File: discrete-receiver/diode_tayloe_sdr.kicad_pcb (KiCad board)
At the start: 2 copper layers, 90 x 90 mm, 0 parts

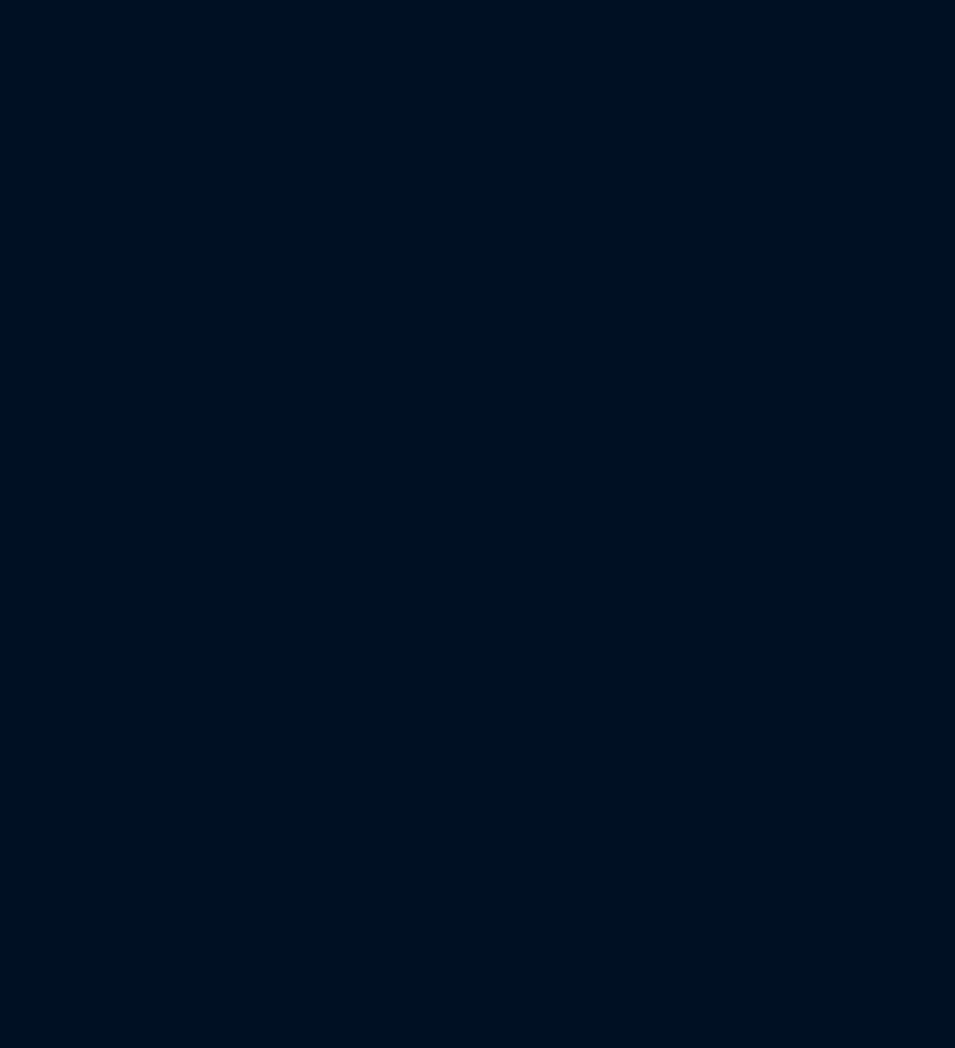
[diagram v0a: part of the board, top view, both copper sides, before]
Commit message: Upgraded to 4 layers, added components. Ready for layout. Only 3 things left on schematic to-do list
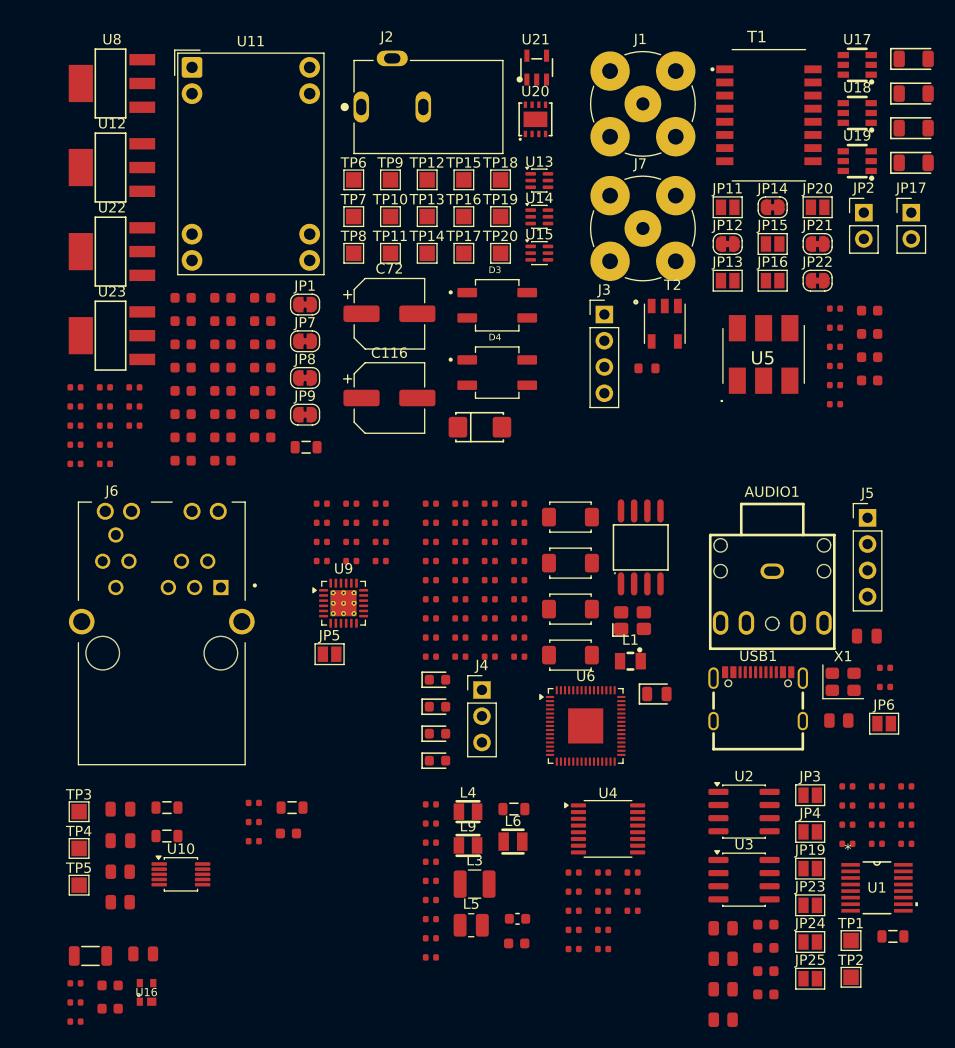
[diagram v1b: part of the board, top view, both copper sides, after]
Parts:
- added AUDIO1: I/Q Out, EasyEDA_Lib:AUDIO-TH_PJ-3126-5A, F.Cu at (215.3, 90.7)
- added C1: 10nF, PCM_JLCPCB:C_0603, F.Cu at (214.7, 122.4)
- added C10: 10uF, PCM_JLCPCB:C_0603, F.Cu at (158.3, 64.0)
- added C100: 100pF, PCM_JLCPCB:C_0603, F.Cu at (168.5, 113.6)
- added C101: 100nF, PCM_JLCPCB:C_0402, F.Cu at (221.4, 66.5)
- added C102: 100pF, PCM_JLCPCB:C_0603, F.Cu at (224.7, 65.3)
- added C103: 100nF, PCM_JLCPCB:C_0402, F.Cu at (221.4, 68.4)
- added C104: 100pF, PCM_JLCPCB:C_0603, F.Cu at (224.7, 67.5)
- added C105: 100nF, PCM_JLCPCB:C_0402, F.Cu at (221.4, 70.2)
- added C106: 100pF, PCM_JLCPCB:C_0603, F.Cu at (224.7, 69.8)
- added C107: 100nF, PCM_JLCPCB:C_0402, F.Cu at (182.3, 125.6)
- added C108: 100pF, PCM_JLCPCB:C_0603, F.Cu at (190.6, 124.2)
- added C109: 10uF, PCM_JLCPCB:C_0603, F.Cu at (166.0, 66.3)
- added C11: 10uF, PCM_JLCPCB:C_0603, F.Cu at (158.3, 66.3)
- added C110: 100nF, PCM_JLCPCB:C_0402, F.Cu at (150.8, 74.1)
- added C111: 100pF, PCM_JLCPCB:C_0603, F.Cu at (166.0, 68.5)
- added C112: 100pF, PCM_JLCPCB:C_0603, F.Cu at (166.0, 70.8)
- added C113: 10uF, PCM_JLCPCB:C_0603, F.Cu at (166.0, 73.0)
- added C114: 100nF, PCM_JLCPCB:C_0402, F.Cu at (150.8, 76.0)
- added C115: 100pF, PCM_JLCPCB:C_0603, F.Cu at (166.0, 75.3)
- added C116: 100uF 25V, Capacitor_SMD:CP_Elec_6.3x7.7, F.Cu at (178.3, 71.5)
- added C12: 100nF, PCM_JLCPCB:C_0805, F.Cu at (154.5, 125.2)
- added C13: 100nF, PCM_JLCPCB:C_0402, F.Cu at (182.3, 81.7)
- added C14: 33pF, PCM_JLCPCB:C_0402, F.Cu at (182.3, 83.5)
- added C15: 4.7uF, PCM_JLCPCB:C_0402, F.Cu at (182.3, 85.4)
- added C16: 4.7uF, PCM_JLCPCB:C_0402, F.Cu at (182.3, 87.2)
- added C17: 33pF, PCM_JLCPCB:C_0402, F.Cu at (182.3, 89.1)
- added C18: 4.7uF, PCM_JLCPCB:C_0402, F.Cu at (182.3, 90.9)
- added C19: 100nF, PCM_JLCPCB:C_0402, F.Cu at (182.3, 92.8)
- added C2: 10nF, PCM_JLCPCB:C_0603, F.Cu at (214.7, 124.7)
- added C20: 4.7uF, PCM_JLCPCB:C_0402, F.Cu at (182.3, 94.6)
- added C21: 100nF, PCM_JLCPCB:C_0402, F.Cu at (182.3, 96.5)
- added C22: 4.7uF, PCM_JLCPCB:C_0402, F.Cu at (185.2, 81.7)
- added C23: 4.7uF, PCM_JLCPCB:C_0402, F.Cu at (185.2, 83.5)
- added C24: 4.7uF, PCM_JLCPCB:C_0402, F.Cu at (185.2, 85.4)
- added C25: 4.7uF, PCM_JLCPCB:C_0402, F.Cu at (185.2, 87.2)
- added C26: 4.7uF, PCM_JLCPCB:C_0402, F.Cu at (185.2, 89.1)
- added C27: 4.7uF, PCM_JLCPCB:C_0402, F.Cu at (185.2, 90.9)
- added C28: 4.7uF, PCM_JLCPCB:C_0402, F.Cu at (185.2, 92.8)
- added C29: 4.7uF, PCM_JLCPCB:C_0402, F.Cu at (185.2, 94.6)
- added C3: 10nF, PCM_JLCPCB:C_0603, F.Cu at (214.7, 126.9)
- added C30: 4.7uF, PCM_JLCPCB:C_0402, F.Cu at (185.2, 96.5)
- added C31: 4.7uF, PCM_JLCPCB:C_0402, F.Cu at (188.0, 81.7)
- added C32: 100pF, PCM_JLCPCB:C_0603, F.Cu at (158.3, 68.5)
- added C33: 100nF, PCM_JLCPCB:C_0402, F.Cu at (147.9, 70.4)
- added C34: 10uF, PCM_JLCPCB:C_0603, F.Cu at (158.3, 70.8)
- added C35: 100nF, PCM_JLCPCB:C_0402, F.Cu at (196.1, 117.4)
- added C36: 1uF, PCM_JLCPCB:C_0402, F.Cu at (196.1, 119.2)
- added C37: 100nF, PCM_JLCPCB:C_0402, F.Cu at (196.1, 121.1)
- added C38: 1uF, PCM_JLCPCB:C_0402, F.Cu at (196.1, 122.9)
- added C39: 100nF, PCM_JLCPCB:C_0402, F.Cu at (196.1, 124.8)
- added C4: 10nF, PCM_JLCPCB:C_0603, F.Cu at (214.7, 129.2)
- added C40: 1uF, PCM_JLCPCB:C_0402, F.Cu at (199.0, 117.4)
- added C41: 100nF, PCM_JLCPCB:C_0402, F.Cu at (199.0, 119.2)
- added C42: 100nF, PCM_JLCPCB:C_0402, F.Cu at (199.0, 121.1)
- added C43: 1uF, PCM_JLCPCB:C_0402, F.Cu at (199.0, 122.9)
- added C44: 100nF, PCM_JLCPCB:C_0402, F.Cu at (199.0, 124.8)
- added C45: 1uF, PCM_JLCPCB:C_0402, F.Cu at (201.8, 117.4)
- added C46: 100nF, PCM_JLCPCB:C_0805, F.Cu at (152.3, 111.2)
- added C47: 100nF, PCM_JLCPCB:C_0805, F.Cu at (152.3, 114.3)
- added C48: 100nF, PCM_JLCPCB:C_0805, F.Cu at (224.5, 94.5)
- added C49: 10pF, PCM_JLCPCB:C_0402, F.Cu at (171.8, 81.7)
- added C5: 100nF, PCM_JLCPCB:C_0402, F.Cu at (222.6, 109.0)
- added C50: 1uF, PCM_JLCPCB:C_0402, F.Cu at (171.8, 83.5)
- added C51: 470pF, PCM_JLCPCB:C_0402, F.Cu at (171.8, 85.4)
- added C52: 1uF, PCM_JLCPCB:C_0402, F.Cu at (171.8, 87.2)
- added C53: 100nF, PCM_JLCPCB:C_0402, F.Cu at (174.6, 81.7)
- added C54: 100nF, PCM_JLCPCB:C_0402, F.Cu at (174.6, 83.5)
- added C55: 100nF, PCM_JLCPCB:C_0402, F.Cu at (147.9, 72.3)
- added C56: 100nF, PCM_JLCPCB:C_0402, F.Cu at (147.9, 128.1)
- added C57: 100nF, PCM_JLCPCB:C_0402, F.Cu at (147.9, 129.9)
- added C58: 51pF, PCM_JLCPCB:C_0402, F.Cu at (182.3, 112.6)
- added C59: 20pF, PCM_JLCPCB:C_0402, F.Cu at (182.3, 114.5)
- added C6: 10pF, PCM_JLCPCB:C_0402, F.Cu at (182.3, 110.8)
- added C60: 10uF, PCM_JLCPCB:C_0603, F.Cu at (158.3, 73.0)
- added C61: 91pF, PCM_JLCPCB:C_0402, F.Cu at (182.3, 116.3)
- added C62: 39pF, PCM_JLCPCB:C_0402, F.Cu at (182.3, 118.2)
- added C63: 68pF, PCM_JLCPCB:C_0402, F.Cu at (182.3, 120.0)
- added C64: 82pF, PCM_JLCPCB:C_0402, F.Cu at (182.3, 121.9)
- added C65: 91pF, PCM_JLCPCB:C_0402, F.Cu at (165.2, 110.6)
- added C66: 91pF, PCM_JLCPCB:C_0402, F.Cu at (165.2, 112.5)
- added C67: 10uF, PCM_JLCPCB:C_0603, F.Cu at (158.3, 75.3)
- added C68: 10uF, PCM_JLCPCB:C_0402, F.Cu at (222.6, 112.7)
- added C69: 1uF, PCM_JLCPCB:C_0402, F.Cu at (222.6, 114.6)
- added C7: 10uF, PCM_JLCPCB:C_0603, F.Cu at (151.3, 128.3)
- added C70: 100nF, PCM_JLCPCB:C_0402, F.Cu at (147.9, 74.1)
- added C71: 100nF, PCM_JLCPCB:C_0402, F.Cu at (147.9, 76.0)
- added C72: 100uF 25V, Capacitor_SMD:CP_Elec_6.3x7.7, F.Cu at (178.3, 63.3)
- added C73: 100pF, PCM_JLCPCB:C_0603, F.Cu at (158.3, 77.5)
- added C74: 100nF, PCM_JLCPCB:C_0402, F.Cu at (147.9, 77.8)
- added C75: 10uF, PCM_JLCPCB:C_0603, F.Cu at (162.2, 61.8)
- added C76: 100pF, PCM_JLCPCB:C_0603, F.Cu at (162.2, 64.0)
- added C77: 100pF, PCM_JLCPCB:C_0603, F.Cu at (162.2, 66.3)
- added C78: 10uF, PCM_JLCPCB:C_0603, F.Cu at (162.2, 68.5)
- added C79: 1uF, PCM_JLCPCB:C_0402, F.Cu at (225.4, 109.0)
- added C8: 100nF, PCM_JLCPCB:C_0402, F.Cu at (222.6, 110.9)
- added C80: 43pF 1%, PCM_JLCPCB:C_0402, F.Cu at (225.4, 110.9)
- added C81: 43pF 1%, PCM_JLCPCB:C_0402, F.Cu at (225.4, 112.7)
- added C82: 1uF, PCM_JLCPCB:C_0402, F.Cu at (225.4, 114.6)
- added C83: 100nF, PCM_JLCPCB:C_0402, F.Cu at (228.3, 109.0)
- added C84: 1uF, PCM_JLCPCB:C_0402, F.Cu at (228.3, 110.9)
- added C85: 100pF, PCM_JLCPCB:C_0603, F.Cu at (162.2, 70.8)
- added C86: 100pF, PCM_JLCPCB:C_0603, F.Cu at (224.7, 63.0)
- added C87: 100nF, PCM_JLCPCB:C_0402, F.Cu at (221.4, 62.8)
- added C88: 100nF, PCM_JLCPCB:C_0402, F.Cu at (147.9, 131.8)
- added C89: 43pF 1%, PCM_JLCPCB:C_0402, F.Cu at (182.3, 123.7)
- added C9: 10uF, PCM_JLCPCB:C_0603, F.Cu at (158.3, 61.8)
- added C90: 100pF, PCM_JLCPCB:C_0603, F.Cu at (162.2, 73.0)
- added C91: 10uF, PCM_JLCPCB:C_0603, F.Cu at (162.2, 75.3)
- added C92: 100nF, PCM_JLCPCB:C_0402, F.Cu at (150.8, 70.4)
- added C93: 100pF, PCM_JLCPCB:C_0603, F.Cu at (162.2, 77.5)
- added C94: 100pF, PCM_JLCPCB:C_0603, F.Cu at (166.0, 61.8)
- added C95: 100nF, PCM_JLCPCB:C_0402, F.Cu at (150.8, 72.3)
- added C96: 10uF, PCM_JLCPCB:C_0603, F.Cu at (166.0, 64.0)
- added C97: 100nF, PCM_JLCPCB:C_0402, F.Cu at (221.4, 64.7)
- added C98: 100pF, PCM_JLCPCB:C_0603, F.Cu at (151.3, 130.5)
- added C99: 100nF, PCM_JLCPCB:C_0402, F.Cu at (165.2, 114.3)
- added D1: Red, PCM_JLCPCB:D_0603, F.Cu at (182.9, 98.7)
- added D10: 1N4004W, PCM_JLCPCB:D_SOD-123FL, F.Cu at (229.0, 42.0)
- added D11: 1N4004W, PCM_JLCPCB:D_SOD-123FL, F.Cu at (229.0, 45.4)
- added D12: 1N4004W, PCM_JLCPCB:D_SOD-123FL, F.Cu at (229.0, 48.7)
- added D13: Green, PCM_JLCPCB:D_0805, F.Cu at (204.2, 100.1)
- added D2: SMAJ58A, PCM_JLCPCB:D_DO-214AC(SMA), F.Cu at (187.1, 74.3)
- added D3: MB10S, sdr_project:SOIC245P670X290-4N, F.Cu at (188.7, 62.5)
- added D4: MB10S, sdr_project:SOIC245P670X290-4N, F.Cu at (188.7, 69.0)
- added D5: Red, PCM_JLCPCB:D_0603, F.Cu at (182.9, 101.3)
- added D7: Red, PCM_JLCPCB:D_0603, F.Cu at (182.9, 103.9)
- added D8: Red, PCM_JLCPCB:D_0603, F.Cu at (182.9, 106.6)
- added D9: 1N4004W, PCM_JLCPCB:D_SOD-123FL, F.Cu at (229.0, 38.7)
- added FB1: ~, PCM_JLCPCB:FB_0805, F.Cu at (227.0, 123.6)
- added FB2: ~, PCM_JLCPCB:FB_0805, F.Cu at (156.8, 111.1)
- added FB4: ~, PCM_JLCPCB:FB_0805, F.Cu at (156.8, 113.8)
- added J1: His Excellence, Connector_Coaxial:BNC_TEConnectivity_1478204_Vertical, F.Cu at (202.8, 43.0)
- added J2: Optional 5V DC Jack, sdr_project:CUI_PJ-102BH, F.Cu at (182.1, 43.3)
- added J3: External Filter, Connector_PinHeader_2.54mm:PinHeader_1x04_P2.54mm_Vertical, F.Cu at (199.1, 63.4)
- added J4: Debug Pins, Connector_PinHeader_2.54mm:PinHeader_1x03_P2.54mm_Vertical, F.Cu at (187.2, 99.7)
- added J5: Display Connector, Connector_PinHeader_2.54mm:PinHeader_1x04_P2.54mm_Vertical, F.Cu at (224.5, 83.1)
- added J6: SI-52003-F, sdr_project:BEL_SI-52003-F, F.Cu at (156.3, 93.1)
- added J7: Her Excellency, Connector_Coaxial:BNC_TEConnectivity_1478204_Vertical, F.Cu at (202.8, 55.1)
- added JP1: 5.65V Jumper, Jumper:SolderJumper-2_P1.3mm_Bridged_RoundedPad1.0x1.5mm, F.Cu at (170.1, 62.4)
- added JP11: SolderJumper_2_Open, Jumper:SolderJumper-2_P1.3mm_Open_Pad1.0x1.5mm, F.Cu at (211.0, 53.0)
- added JP12: SolderJumper_2_Bridged, Jumper:SolderJumper-2_P1.3mm_Bridged_RoundedPad1.0x1.5mm, F.Cu at (211.0, 56.6)
- added JP13: SolderJumper_2_Open, Jumper:SolderJumper-2_P1.3mm_Open_Pad1.0x1.5mm, F.Cu at (211.0, 60.1)
- added JP14: SolderJumper_2_Bridged, Jumper:SolderJumper-2_P1.3mm_Bridged_RoundedPad1.0x1.5mm, F.Cu at (215.4, 53.0)
- added JP15: SolderJumper_2_Open, Jumper:SolderJumper-2_P1.3mm_Open_Pad1.0x1.5mm, F.Cu at (215.4, 56.6)
- added JP16: SolderJumper_2_Open, Jumper:SolderJumper-2_P1.3mm_Open_Pad1.0x1.5mm, F.Cu at (215.4, 60.1)
- added JP17: Jumper_2_Small_Open, Connector_PinHeader_2.54mm:PinHeader_1x02_P2.54mm_Vertical, F.Cu at (228.8, 53.5)
- added JP19: SolderJumper_2_Open, Jumper:SolderJumper-2_P1.3mm_Open_Pad1.0x1.5mm, F.Cu at (219.0, 117.0)
- added JP2: Jumper_2_Small_Open, Connector_PinHeader_2.54mm:PinHeader_1x02_P2.54mm_Vertical, F.Cu at (224.2, 53.5)
- added JP20: SolderJumper_2_Open, Jumper:SolderJumper-2_P1.3mm_Open_Pad1.0x1.5mm, F.Cu at (219.7, 53.0)
- added JP21: SolderJumper_2_Bridged, Jumper:SolderJumper-2_P1.3mm_Bridged_RoundedPad1.0x1.5mm, F.Cu at (219.7, 56.6)
- added JP22: SolderJumper_2_Bridged, Jumper:SolderJumper-2_P1.3mm_Bridged_RoundedPad1.0x1.5mm, F.Cu at (219.7, 60.1)
- added JP23: SolderJumper_2_Open, Jumper:SolderJumper-2_P1.3mm_Open_Pad1.0x1.5mm, F.Cu at (219.0, 120.5)
- added JP24: SolderJumper_2_Open, Jumper:SolderJumper-2_P1.3mm_Open_Pad1.0x1.5mm, F.Cu at (219.0, 124.1)
- added JP25: SolderJumper_2_Open, Jumper:SolderJumper-2_P1.3mm_Open_Pad1.0x1.5mm, F.Cu at (219.0, 127.6)
- added JP3: SolderJumper_2_Open, Jumper:SolderJumper-2_P1.3mm_Open_Pad1.0x1.5mm, F.Cu at (219.0, 109.9)
- added JP4: SolderJumper_2_Open, Jumper:SolderJumper-2_P1.3mm_Open_Pad1.0x1.5mm, F.Cu at (219.0, 113.4)
- added JP5: SolderJumper_2_Open, Jumper:SolderJumper-2_P1.3mm_Open_Pad1.0x1.5mm, F.Cu at (172.5, 96.3)
- added JP6: SolderJumper_2_Open, Jumper:SolderJumper-2_P1.3mm_Open_Pad1.0x1.5mm, F.Cu at (226.1, 103.0)
- added JP7: USB_Jumper, Jumper:SolderJumper-2_P1.3mm_Bridged_RoundedPad1.0x1.5mm, F.Cu at (170.1, 66.0)
- added JP8: DC_Jumper, Jumper:SolderJumper-2_P1.3mm_Bridged_RoundedPad1.0x1.5mm, F.Cu at (170.1, 69.5)
- added JP9: POE_Jumper, Jumper:SolderJumper-2_P1.3mm_Bridged_RoundedPad1.0x1.5mm, F.Cu at (170.1, 73.1)
- added L1: 3.3uH, EasyEDA_Lib:IND-SMD_L2.0-W1.6_AOTA-B201610S3R3-101-T, F.Cu at (201.6, 96.9)
- added L10: 160nH, PCM_JLCPCB:L_0805, F.Cu at (190.3, 111.2)
- added L11: 300nH, PCM_JLCPCB:L_0805, F.Cu at (168.9, 111.1)
- added L12: 2.2uH,50mA, PCM_JLCPCB:L_0805, F.Cu at (170.2, 76.2)
- added L2: 4.7uH,25mA, PCM_JLCPCB:L_1206, F.Cu at (149.4, 125.4)
- added L3: 27nH, Inductor_SMD:L_1210_3225Metric, F.Cu at (186.5, 118.5)
- added L4: 33nH, EasyEDA_Lib:IND-SMD_L2.2-W1.6, F.Cu at (185.9, 111.5)
- added L5: 68nH, Inductor_SMD:L_1008_2520Metric, F.Cu at (186.2, 122.5)
- added L6: 16nH, EasyEDA_Lib:IND-SMD_L2.4-W1.7, F.Cu at (190.2, 114.4)
- added L8: 36nH, PCM_JLCPCB:L_0603, F.Cu at (190.7, 121.9)
- added L9: 18nH, EasyEDA_Lib:IND-SMD_L2.2-W1.6, F.Cu at (185.9, 114.8)
- added R1: 5.1kΩ, PCM_JLCPCB:R_0402, F.Cu at (226.2, 97.6)
- added R10: 10kΩ, PCM_JLCPCB:R_0402, F.Cu at (153.6, 70.4)
- added R11: 330Ω, PCM_JLCPCB:R_0402, F.Cu at (188.0, 94.6)
- added R12: 330Ω, PCM_JLCPCB:R_0402, F.Cu at (188.0, 96.5)
- added R13: 33Ω, PCM_JLCPCB:R_0402, F.Cu at (190.9, 81.7)
- added R14: 47Ω, PCM_JLCPCB:R_0402, F.Cu at (228.3, 112.7)
- added R15: 47Ω, PCM_JLCPCB:R_0402, F.Cu at (228.3, 114.6)
- added R16: 10kΩ, PCM_JLCPCB:R_0402, F.Cu at (190.9, 83.5)
- added R17: 10kΩ, PCM_JLCPCB:R_0402, F.Cu at (190.9, 85.4)
- added R18: 12kΩ, PCM_JLCPCB:R_0402, F.Cu at (174.6, 85.4)
- added R19: 330Ω, PCM_JLCPCB:R_0402, F.Cu at (190.9, 87.2)
- added R2: 1kΩ, PCM_JLCPCB:R_0402, F.Cu at (188.0, 83.5)
- added R20: 10kΩ, PCM_JLCPCB:R_0402, F.Cu at (201.8, 119.2)
- added R21: 10kΩ, PCM_JLCPCB:R_0805, F.Cu at (210.6, 122.8)
- added R22: 10kΩ, PCM_JLCPCB:R_0402, F.Cu at (190.9, 89.1)
- added R23: 4.7kΩ, PCM_JLCPCB:R_0402, F.Cu at (190.9, 90.9)
- added R24: 4.7kΩ, PCM_JLCPCB:R_0402, F.Cu at (190.9, 92.8)
- added R25: 10kΩ, PCM_JLCPCB:R_0402, F.Cu at (174.6, 87.2)
- added R26: 1.5kΩ, PCM_JLCPCB:R_0402, F.Cu at (190.9, 94.6)
- added R27: 10kΩ, PCM_JLCPCB:R_0402, F.Cu at (153.6, 72.3)
- added R28: 10kΩ, PCM_JLCPCB:R_0402, F.Cu at (201.8, 121.1)
- added R29: 10kΩ, PCM_JLCPCB:R_0805, F.Cu at (210.6, 125.7)
- added R3: 49.9kΩ, PCM_JLCPCB:R_0402, F.Cu at (150.8, 77.8)
- added R30: 100Ω, PCM_JLCPCB:R_0402, F.Cu at (177.5, 81.7)
- added R31: 100Ω, PCM_JLCPCB:R_0402, F.Cu at (177.5, 83.5)
- added R32: 10kΩ, PCM_JLCPCB:R_0402, F.Cu at (177.5, 85.4)
- added R33: 10kΩ, PCM_JLCPCB:R_0402, F.Cu at (177.5, 87.2)
- added R34: 33Ω, PCM_JLCPCB:R_0805, F.Cu at (221.8, 102.7)
- added R35: 10kΩ, PCM_JLCPCB:R_0402, F.Cu at (153.6, 74.1)
- added R36: 330Ω, PCM_JLCPCB:R_0402, F.Cu at (190.9, 96.5)
- added R37: 33Ω, PCM_JLCPCB:R_0805, F.Cu at (152.3, 117.3)
- added R38: 33Ω, PCM_JLCPCB:R_0805, F.Cu at (152.3, 120.2)
- added R4: 5.1kΩ, PCM_JLCPCB:R_0402, F.Cu at (226.2, 99.4)
- added R40: 10kΩ, PCM_JLCPCB:R_0805, F.Cu at (210.6, 128.7)
- added R41: 10kΩ, PCM_JLCPCB:R_0805, F.Cu at (210.6, 131.6)
- added R43: 47 1%, PCM_JLCPCB:R_0603, F.Cu at (203.2, 68.6)
- added R46: 10kΩ, PCM_JLCPCB:R_0402, F.Cu at (221.4, 72.1)
- added R5: 1kΩ, PCM_JLCPCB:R_0402, F.Cu at (188.0, 85.4)
- added R6: 10kΩ, PCM_JLCPCB:R_0402, F.Cu at (188.0, 87.2)
- added R7: 1kΩ, PCM_JLCPCB:R_0402, F.Cu at (188.0, 89.1)
- added R8: 47Ω, PCM_JLCPCB:R_0402, F.Cu at (188.0, 90.9)
- added R9: 47Ω, PCM_JLCPCB:R_0402, F.Cu at (188.0, 92.8)
- added S1: Tactile Button, 160gf, PCM_JLCPCB:SW_TS-1088-AR02016, F.Cu at (195.8, 83.0)
- added S2: Tactile Button, 160gf, PCM_JLCPCB:SW_TS-1088-AR02016, F.Cu at (195.8, 87.4)
- added S3: Tactile Button, 160gf, PCM_JLCPCB:SW_TS-1088-AR02016, F.Cu at (195.8, 91.9)
- added S4: Tactile Button, 160gf, PCM_JLCPCB:SW_TS-1088-AR02016, F.Cu at (195.8, 96.3)
- added T1: H1102NLT, sdr_project:XFMR_H1102NLT, F.Cu at (215.0, 44.1)
- added T2: MABA-007159-000000, sdr_project:XFMR_MABA-007159-000000, F.Cu at (204.9, 64.3)
- added TP1: I_out, TestPoint:TestPoint_Pad_1.5x1.5mm, F.Cu at (222.9, 124.0)
- added TP10: +3.3V, TestPoint:TestPoint_Pad_1.5x1.5mm, F.Cu at (178.4, 53.9)
- added TP11: USB_IN, TestPoint:TestPoint_Pad_1.5x1.5mm, F.Cu at (178.4, 57.5)
- added TP12: POE_IN, TestPoint:TestPoint_Pad_1.5x1.5mm, F.Cu at (181.9, 50.4)
- added TP13: +4.8V_A, TestPoint:TestPoint_Pad_1.5x1.5mm, F.Cu at (181.9, 53.9)
- added TP14: +2.4V_A, TestPoint:TestPoint_Pad_1.5x1.5mm, F.Cu at (181.9, 57.5)
- added TP15: +3.3V_ADC, TestPoint:TestPoint_Pad_1.5x1.5mm, F.Cu at (185.5, 50.4)
- added TP16: POE_Raw, TestPoint:TestPoint_Pad_1.5x1.5mm, F.Cu at (185.5, 53.9)
- added TP17: POE+, TestPoint:TestPoint_Pad_1.5x1.5mm, F.Cu at (185.5, 57.5)
- added TP18: POE-, TestPoint:TestPoint_Pad_1.5x1.5mm, F.Cu at (189.0, 50.4)
- added TP19: +3.3V_SI5351, TestPoint:TestPoint_Pad_1.5x1.5mm, F.Cu at (189.0, 53.9)
- added TP2: Q_out, TestPoint:TestPoint_Pad_1.5x1.5mm, F.Cu at (222.9, 127.5)
- added TP20: +3.3V_CLK, TestPoint:TestPoint_Pad_1.5x1.5mm, F.Cu at (189.0, 57.5)
- added TP3: I LO, TestPoint:TestPoint_Pad_1.5x1.5mm, F.Cu at (148.3, 111.5)
- added TP4: Q LO, TestPoint:TestPoint_Pad_1.5x1.5mm, F.Cu at (148.3, 115.0)
- added TP5: OSC, TestPoint:TestPoint_Pad_1.5x1.5mm, F.Cu at (148.3, 118.6)
- added TP6: DC_IN, TestPoint:TestPoint_Pad_1.5x1.5mm, F.Cu at (174.8, 50.4)
- added TP7: VIN, TestPoint:TestPoint_Pad_1.5x1.5mm, F.Cu at (174.8, 53.9)
- added TP8: GND, TestPoint:TestPoint_Pad_1.5x1.5mm, F.Cu at (174.8, 57.5)
- added TP9: +5V, TestPoint:TestPoint_Pad_1.5x1.5mm, F.Cu at (178.4, 50.4)
- added U1: SN74CBT3253DBQR, sdr_project:SN74CBT3253DBQ16, F.Cu at (225.5, 118.9)
- added U10: MS5351M, Package_SO:MSOP-10_3x3mm_P0.5mm, F.Cu at (158.1, 117.5)
- added U11: Ag9905LP, Converter_DCDC:Converter_DCDC_Silvertel_Ag99xxLP_THT, F.Cu at (159.2, 39.5)
- added U12: ~, EasyEDA_Lib:SOT-223-3_L6.5-W3.4-P2.30-LS7.0-BR, F.Cu at (151.4, 49.2)
- added U13: LM66100DCK, Package_TO_SOT_SMD:SOT-363_SC-70-6, F.Cu at (192.8, 50.4)
- added U14: LM66100DCK, Package_TO_SOT_SMD:SOT-363_SC-70-6, F.Cu at (192.8, 54.0)
- added U15: LM66100DCK, Package_TO_SOT_SMD:SOT-363_SC-70-6, F.Cu at (192.8, 57.5)
- added U16: PSA4-5043_, sdr_project:PSA4-5043_, F.Cu at (154.8, 129.0)
- added U17: ~, EasyEDA_Lib:SOT-23-6_L2.9-W1.6-P0.95-LS2.8-BR, F.Cu at (223.5, 39.3)
- added U18: ~, EasyEDA_Lib:SOT-23-6_L2.9-W1.6-P0.95-LS2.8-BR, F.Cu at (223.5, 43.9)
- added U19: ~, EasyEDA_Lib:SOT-23-6_L2.9-W1.6-P0.95-LS2.8-BR, F.Cu at (223.5, 48.6)
- added U2: OPA1612AxD, Package_SO:SOIC-8_3.9x4.9mm_P1.27mm, F.Cu at (212.6, 111.5)
- added U20: ~, EasyEDA_Lib:TDFN-8_L3.0-W3.0-P0.65-BL-EP2.3, F.Cu at (192.4, 44.5)
- added U21: ~, EasyEDA_Lib:SOT-23-5_L3.0-W1.7-P0.95-LS2.8-BL, F.Cu at (192.5, 39.5)
- added U22: ~, EasyEDA_Lib:SOT-223-3_L6.5-W3.4-P2.30-LS7.0-BR, F.Cu at (151.4, 57.3)
- added U23: ~, EasyEDA_Lib:SOT-223-3_L6.5-W3.4-P2.30-LS7.0-BR, F.Cu at (151.4, 65.4)
- added U3: OPA1612AxD, Package_SO:SOIC-8_3.9x4.9mm_P1.27mm, F.Cu at (212.6, 118.1)
- added U4: CJC5340, Package_SO:TSSOP-16_4.4x5mm_P0.65mm, F.Cu at (199.4, 113.2)
- added U5: ADE-1+, sdr_project:ADE12, F.Cu at (214.5, 67.3)
- added U6: RP2350A, Package_DFN_QFN:QFN-60-1EP_7x7mm_P0.4mm_EP3.4x3.4mm, F.Cu at (197.3, 103.2)
- added U7: W25Q128, PCM_JLCPCB:SOIC-8_L5.3-W5.3-P1.27-LS8.0-BL, F.Cu at (202.6, 85.9)
- added U8: ~, EasyEDA_Lib:SOT-223-3_L6.5-W3.4-P2.30-LS7.0-BR, F.Cu at (151.4, 41.1)
- added U9: LAN8720A, Package_DFN_QFN:VQFN-24-1EP_4x4mm_P0.5mm_EP2.5x2.5mm_ThermalVias, F.Cu at (173.9, 91.3)
- added USB1: ~, EasyEDA_Lib:USB-C-SMD_TYPE-C16PIN_C668624, F.Cu at (214.0, 100.4)
- added X1: YC24.576MUBCE2O, Oscillator:Oscillator_SMD_Abracon_ASE-4Pin_3.2x2.5mm, F.Cu at (222.2, 98.9)
- added X2: X322512MSB4SI, PCM_JLCPCB:CRYSTAL-SMD_4P-L3.2-W2.5-BL, F.Cu at (201.8, 93.0)
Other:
- copper layers 2 -> 4

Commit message: Initial changes to PCB
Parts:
- moved J6 121.5 mm to (44.6, 45.1), turned to 180 degrees

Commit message: :)
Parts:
- removed J1: His Excellence, Connector_Coaxial:BNC_TEConnectivity_1478204_Vertical
- removed J7: Her Excellency, Connector_Coaxial:BNC_TEConnectivity_1478204_Vertical
- added D6: White, PCM_JLCPCB:D_0603, F.Cu at (127.1, 166.9)
- added D7: Yellow, PCM_JLCPCB:D_0603, F.Cu at (127.1, 169.5)
- added R39: 100Ω, PCM_JLCPCB:R_0402, F.Cu at (130.5, 166.5)
- added RF1: 3GHz, EasyEDA_Lib:BNC-TH_DOSIN-801-0051, F.Cu at (131.0, 145.5)
- added RF2: 3GHz, EasyEDA_Lib:BNC-TH_DOSIN-801-0051, F.Cu at (131.0, 157.5)
- moved J6 102.9 mm to (144.0, 18.5)
- moved J2 36.3 mm to (163.9, 11.9), turned to 90 degrees
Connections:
- U6 pad 34: unconnected-(U6-GPIO22-Pad34) -> Net-(J8-Pin_1)
- U6 pad 36: unconnected-(U6-GPIO24-Pad36) -> Net-(J8-Pin_2)
- U6 pad 37: unconnected-(U6-GPIO25-Pad37) -> Net-(J8-Pin_3)
- U6 pad 41: unconnected-(U6-GPIO27/ADC1-Pad41) -> Net-(J8-Pin_4)
- U6 pad 42: unconnected-(U6-GPIO28/ADC2-Pad42) -> Net-(J8-Pin_5)

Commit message: PCB edge cuts finalized
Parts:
- added H1: MountingHole, MountingHole:MountingHole_3.2mm_M3, F.Cu at (37.5, 36.5)
- added H2: MountingHole, MountingHole:MountingHole_3.2mm_M3, F.Cu at (137.5, 36.5)
- added H3: MountingHole, MountingHole:MountingHole_3.2mm_M3, F.Cu at (37.5, 136.5)
- added H4: MountingHole, MountingHole:MountingHole_3.2mm_M3, F.Cu at (137.5, 136.5)
- moved C108 23.9 mm to (214.4, 126.7)
- moved C109 23.9 mm to (189.8, 68.8)
- moved C111 23.9 mm to (189.8, 71.0)
- moved C112 23.9 mm to (189.8, 73.2)
- moved C113 23.9 mm to (189.8, 75.5)
- moved C115 23.9 mm to (189.8, 77.8)
- moved C116 23.9 mm to (202.1, 73.9)
- moved C12 23.9 mm to (178.3, 127.7)
- moved C22 23.9 mm to (209.0, 84.2)
- moved C23 23.9 mm to (209.0, 86.0)
- moved C24 23.9 mm to (209.0, 87.9)
- moved C25 23.9 mm to (209.0, 89.7)
- moved C26 23.9 mm to (209.0, 91.6)
- moved C27 23.9 mm to (209.0, 93.4)
- moved C28 23.9 mm to (209.0, 95.3)
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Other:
- board size 90 x 90 mm -> 110 x 110 mm

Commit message: Made changes to schematic
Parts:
- moved AUDIO1 167.0 mm to (81.5, 38.0)
- moved USB1 156.6 mm to (96.3, 35.5), turned to 180 degrees
- moved J2 122.4 mm to (67.0, 35.0)
- moved J6 118.9 mm to (50.7, 41.5)

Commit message: :)
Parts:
- removed C69, C79: 1uF, PCM_JLCPCB:C_0402
- removed the D7 at (206.7, 106.4)
- removed the D7 at (150.9, 171.9)
- removed D8: Red, PCM_JLCPCB:D_0603
- removed R36: 330Ω, PCM_JLCPCB:R_0402
- removed TP10: +3.3V, TestPoint:TestPoint_Pad_1.5x1.5mm
- removed TP11: USB_IN, TestPoint:TestPoint_Pad_1.5x1.5mm
- removed TP12: POE_IN, TestPoint:TestPoint_Pad_1.5x1.5mm
- removed TP13: +4.8V_A, TestPoint:TestPoint_Pad_1.5x1.5mm
- removed TP14: +2.4V_A, TestPoint:TestPoint_Pad_1.5x1.5mm
- removed TP15: +3.3V_ADC, TestPoint:TestPoint_Pad_1.5x1.5mm
- removed TP19: +3.3V_SI5351, TestPoint:TestPoint_Pad_1.5x1.5mm
- removed TP20: +3.3V_CLK, TestPoint:TestPoint_Pad_1.5x1.5mm
- removed TP5: OSC, TestPoint:TestPoint_Pad_1.5x1.5mm
- removed TP6: DC_IN, TestPoint:TestPoint_Pad_1.5x1.5mm
- removed TP7: VIN, TestPoint:TestPoint_Pad_1.5x1.5mm
- removed TP9: +5V, TestPoint:TestPoint_Pad_1.5x1.5mm
- added C117: 10uF, PCM_JLCPCB:C_0603, F.Cu at (182.3, 108.8)
- added C118: 10uF, PCM_JLCPCB:C_0603, F.Cu at (182.3, 111.1)
- added D7: Yellow, PCM_JLCPCB:D_0603, F.Cu at (222.1, 121.1)
- added JP10: ~, Jumper:SolderJumper-2_P1.3mm_Bridged_RoundedPad1.0x1.5mm, F.Cu at (209.1, 71.3)
- added JP18: ~, Jumper:SolderJumper-2_P1.3mm_Bridged_RoundedPad1.0x1.5mm, F.Cu at (209.1, 74.8)
- added JP26: ~, Jumper:SolderJumper-2_P1.3mm_Bridged_RoundedPad1.0x1.5mm, F.Cu at (209.1, 78.4)
- added JP27: ~, Jumper:SolderJumper-2_P1.3mm_Bridged_RoundedPad1.0x1.5mm, F.Cu at (209.1, 81.9)
- added JP28: ~, Jumper:SolderJumper-2_P1.3mm_Bridged_RoundedPad1.0x1.5mm, F.Cu at (213.4, 71.3)
- added JP29: ~, Jumper:SolderJumper-2_P1.3mm_Bridged_RoundedPad1.0x1.5mm, F.Cu at (213.4, 74.8)
- added JP30: ~, Jumper:SolderJumper-2_P1.3mm_Bridged_RoundedPad1.0x1.5mm, F.Cu at (213.4, 78.4)
- added R42: 33Ω, PCM_JLCPCB:R_0805, F.Cu at (202.8, 124.7)
- moved R39 95.3 mm to (230.0, 111.1)
- moved D6 87.5 mm to (222.1, 118.5)
- moved J5 80.7 mm to (178.3, 125.6)
- moved C48 73.0 mm to (182.8, 129.4)
- moved R34 68.4 mm to (182.8, 132.4)
- moved JP6 68.4 mm to (187.2, 132.7)
- moved R1 67.3 mm to (187.3, 124.2)
- moved R4 67.3 mm to (187.3, 126.1)
- moved X1 67.3 mm to (183.2, 125.6)
- moved TP1 65.8 mm to (182.1, 114.0)
- moved TP2 65.8 mm to (182.1, 117.5)
- moved JP19 65.7 mm to (178.2, 107.6)
- moved JP23 65.7 mm to (178.2, 111.1)
- moved JP24 65.7 mm to (178.2, 114.7)
- moved JP25 65.7 mm to (178.2, 118.2)
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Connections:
- R27 pad 1: +4.8V_A -> Net-(JP30-B)
- R3 pad 2: +4.8V_A -> Net-(JP30-B)
- U10 pad 6: /Clock Generator/CLK_2 -> Net-(JP31-B)
- U12 pad 2: +3.3V_ADC -> Net-(JP26-B)
- U12 pad 4: +3.3V_ADC -> Net-(JP26-B)
- U13 pad 3: +5V -> Net-(JP10-B)
- U13 pad 6: +5V -> Net-(JP10-B)
- U14 pad 3: +5V -> Net-(JP10-B)
- U14 pad 6: +5V -> Net-(JP10-B)
- U15 pad 3: +5V -> Net-(JP10-B)
- U15 pad 6: +5V -> Net-(JP10-B)
- U20 pad 1: +4.8V_A -> Net-(JP30-B)
- U20 pad 2: +4.8V_A -> Net-(JP30-B)
- U21 pad 1: +2.4V_A -> Net-(JP29-B)
- U21 pad 4: +2.4V_A -> Net-(JP29-B)
- U21 pad 5: +4.8V_A -> Net-(JP30-B)
- U22 pad 2: +3.3V_SI5351 -> Net-(JP27-B)
- U22 pad 4: +3.3V_SI5351 -> Net-(JP27-B)
- U23 pad 2: +3.3V_CLK -> Net-(JP28-B)
- U23 pad 4: +3.3V_CLK -> Net-(JP28-B)
- U8 pad 2: +3.3V -> Net-(JP18-B)
- U8 pad 4: +3.3V -> Net-(JP18-B)
